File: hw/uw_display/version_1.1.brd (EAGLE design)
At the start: 89.4 x 94.4 mm, 99 parts, among them J2 SWD, J4 USB, J5 UART, U1 LPC1785, U2 MCP2551, U3 AS4C4M16SA, U4 W25Q32FV, U5 MIC5247-1.8YM5, U6 TVP5150AM1, U7 TVP5150AM1, X1 20MHz, X2 34.768kHz, X3 14.31MHz, X4 14.31 MHz, Y1 BUZZER

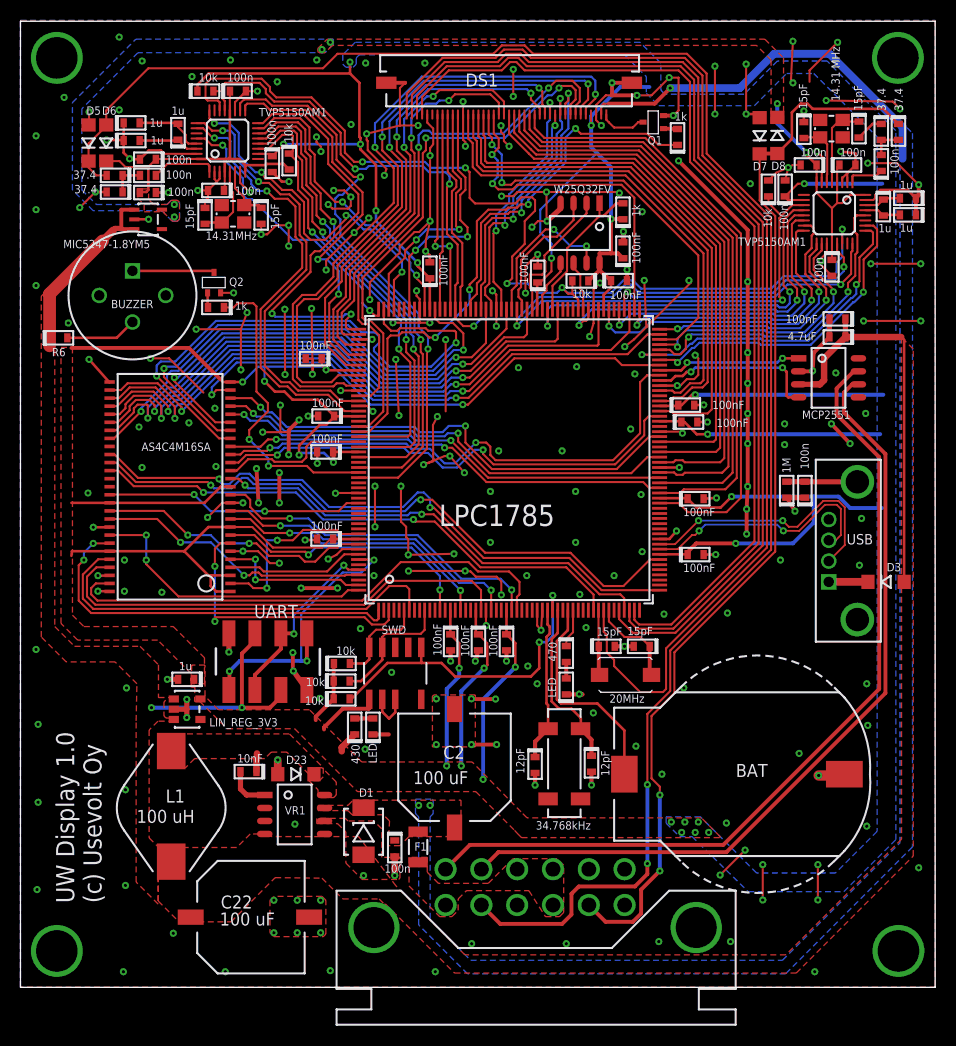
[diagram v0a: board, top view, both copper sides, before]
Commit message: Start developing the display SW
   - Testing freertos
   - UART, timers and gpios are working
   - Add uGUI library to ui directory
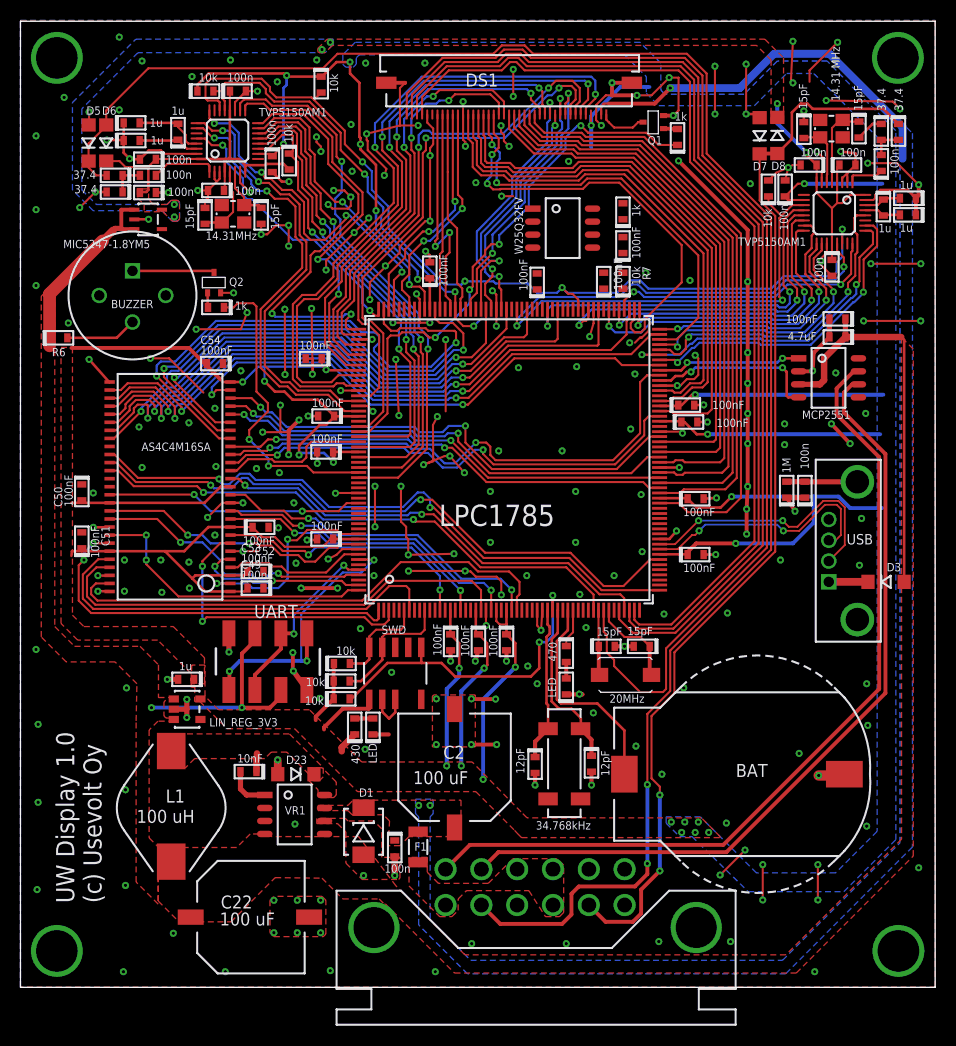
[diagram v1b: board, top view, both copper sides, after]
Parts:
- added C49, C50, C51, C52, C53, C54: 100nF, usevolt:0603_SILKSCREEN
- added R7: 10k, usevolt:0603_SILKSCREEN
- moved R19 32.1 mm to (68.0, 94.0), turned to 90 degrees
- moved U4 1.88 mm to (91.0, 79.1), turned to 0 degrees
- moved C4 1.31 mm to (95.6, 74.4), turned to 270 degrees
- moved C3 0.69 mm to (89.1, 74.4)
- moved C23 0.51 mm to (97.5, 77.9)
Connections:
- new net ISP: R7.1, U1.110
- net +3V3: now also C49.0, C50.0, C51.1, C52.1, C53.0, C54.0, R7.0, U1.24
- net GND: now also C49.1, C50.1, C51.0, C52.0, C53.1, C54.1
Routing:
- net GND: track 507.2 -> 452.0 mm, vias 277 -> 275
- net +3V3: track 383.3 -> 352.6 mm, vias 30 -> 29
- net SPIFI_IO3: track 15.5 -> 0.00 mm, vias 2 -> 0
- net SPIFI_CS: track 15.1 -> 0.00 mm
- net SPIFI_IO1: track 13.5 -> 0.00 mm
- net SPIFI_IO2: track 13.4 -> 0.00 mm
- net LCD_VD18: track 33.4 -> 42.8 mm
- net I2C_SDA: track 98.4 -> 89.7 mm, vias 5 -> 4
- net SPIFI_IO0: track 5.26 -> 0.00 mm
- net I2C_SCL: track 89.8 -> 84.9 mm
- net SPIFI_CLK: track 4.91 -> 0.00 mm
- net EMC_D2: track 14.7 -> 17.0 mm
- net EMC_D0: track 18.0 -> 20.2 mm
- net LCD_DE: track 20.6 -> 22.8 mm
- net LCD_DCLK: track 24.4 -> 22.3 mm
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
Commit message: Display runs now with uw_bootloader
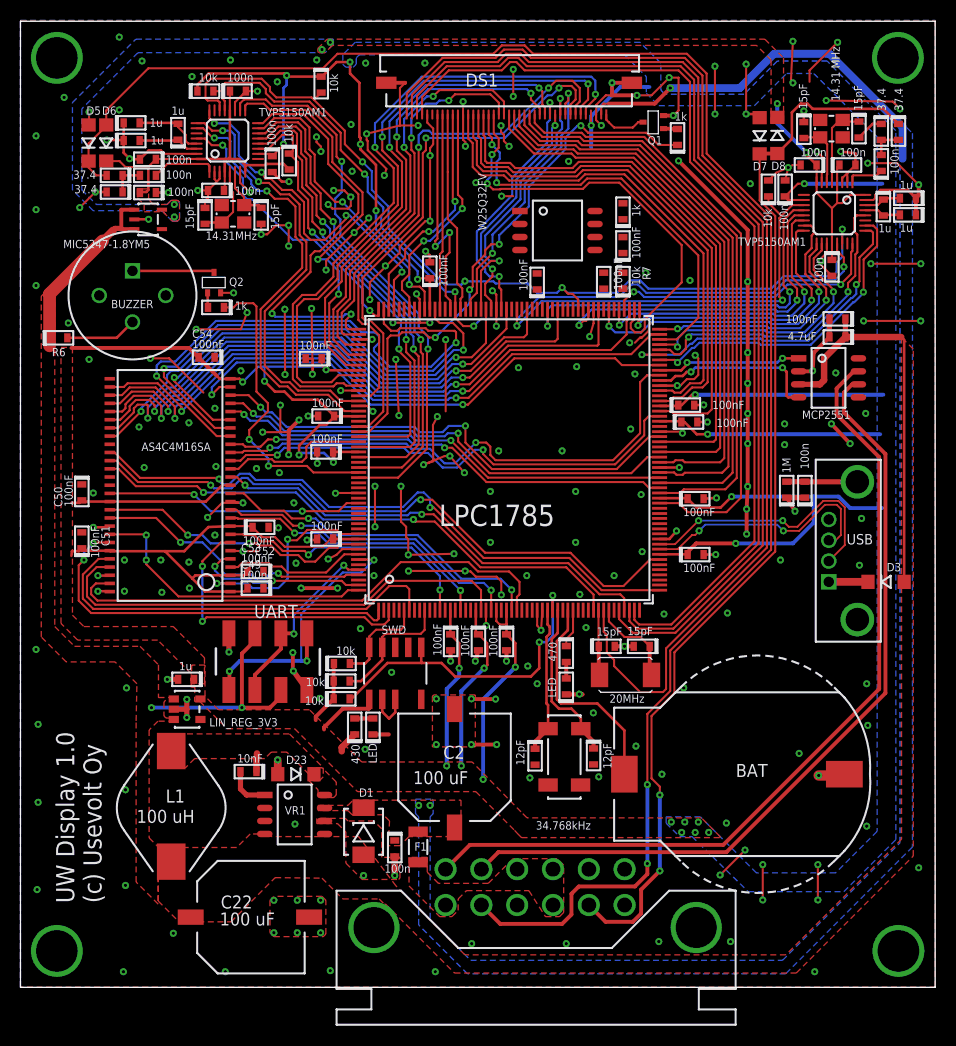
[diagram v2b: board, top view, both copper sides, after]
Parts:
- U4: device usevolt:SOIC8 -> usevolt:SOIC8_W
- moved U4 4.26 mm to (87.4, 81.5)
- moved C54 1.02 mm to (57.0, 67.2)
- moved C20 0.81 mm to (88.9, 28.3)
- moved C19 0.74 mm to (94.6, 28.3)
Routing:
- net GND: track 452.0 -> 446.6 mm
- net +3V3: track 352.6 -> 353.6 mm
- net N$7: track 15.2 -> 14.3 mm
- net N$8: track 16.8 -> 16.2 mm

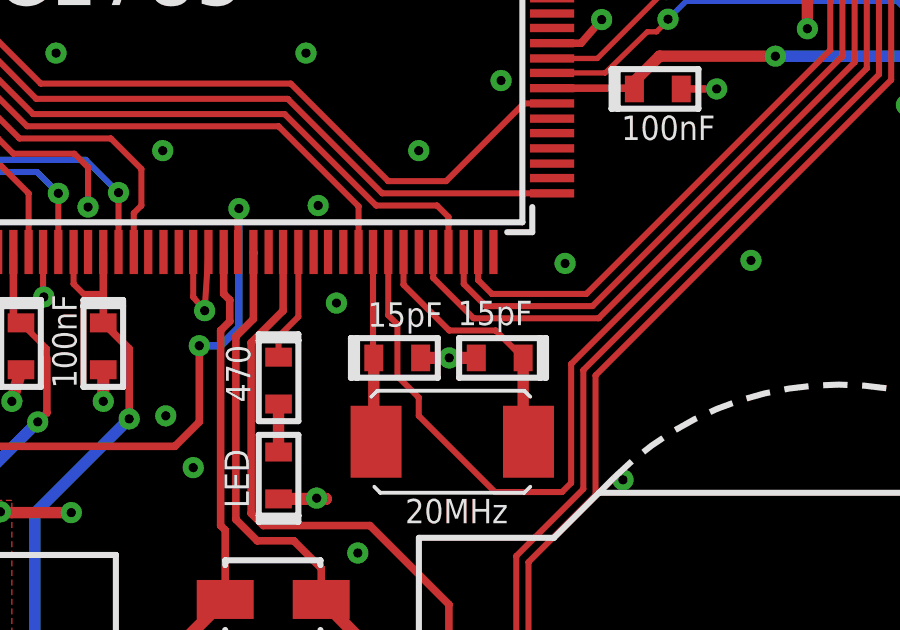
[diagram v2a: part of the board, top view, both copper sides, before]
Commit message: Corrected HW connector bolt sizes
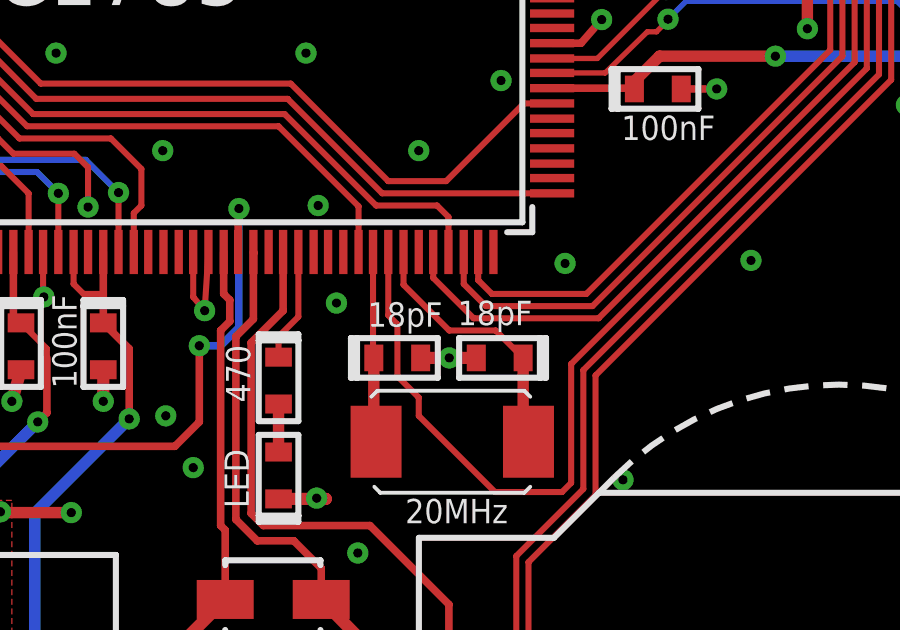
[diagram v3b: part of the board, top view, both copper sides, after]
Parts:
- C5, C6: value 15pF -> 18pF
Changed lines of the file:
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@@
 <?xml version="1.0" encoding="utf-8"?>
 <!DOCTYPE eagle SYSTEM "eagle.dtd">
-<eagle version="7.2.0">
+<eagle version="7.6.0">
 <drawing>
 <settings>
@@
 <setting verticaltext="up"/>
 </settings>
-<grid distance="4" unitdist="mil" unit="mil" style="lines" multiple="1" display="no" altdistance="1" altunitdist="mil" altunit="mil"/>
+<grid distance="0.2" unitdist="mm" unit="mm" style="dots" multiple="1" display="yes" altdistance="1" altunitdist="mil" altunit="mil"/>
 <layers>
 <layer number="1" name="Top" color="4" fill="1" visible="yes" active="yes"/>
@@
 <attribute name="VALUE" x="124.5362" y="79.4258" size="0.8128" layer="21" font="vector"/>
 </element>
-<element name="C5" library="usevolt" package="0603_SILKSCREEN" value="15pF" x="95.7072" y="38.9128" smashed="yes" rot="R180">
+<element name="C5" library="usevolt" package="0603_SILKSCREEN" value="18pF" x="95.7072" y="38.9128" smashed="yes" rot="R180">
 <attribute name="SMD_SIZE" value="0603 (1608 metric)" x="95.7072" y="38.9128" size="1.778" layer="27" rot="R180" display="off"/>
 <attribute name="VALUE" x="97.409" y="40.767" size="0.8128" layer="21" font="vector" rot="R180"/>
 </element>
-<element name="C6" library="usevolt" package="0603_SILKSCREEN" value="15pF" x="99.5172" y="38.9128" smashed="yes">
+<element name="C6" library="usevolt" package="0603_SILKSCREEN" value="18pF" x="99.5172" y="38.9128" smashed="yes">
 <attribute name="SMD_SIZE" value="0603 (1608 metric)" x="99.5172" y="38.9128" size="1.778" layer="27" display="off"/>
 <attribute name="VALUE" x="97.917" y="40.005" size="0.8128" layer="21" font="vector"/>
